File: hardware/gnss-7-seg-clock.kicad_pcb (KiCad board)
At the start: 2 copper layers, 225 x 63.5 mm, 90 parts, among them J1 USB4105-GF-A, J2 Conn_Coaxial, J3 Conn_01x03, SW1 SW_Push, SW2 SW_Push, SW3 SW_Push, SW4 SW_Push, SW5 SW_Push, U1 SA15-11GWA, U10 RP2040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

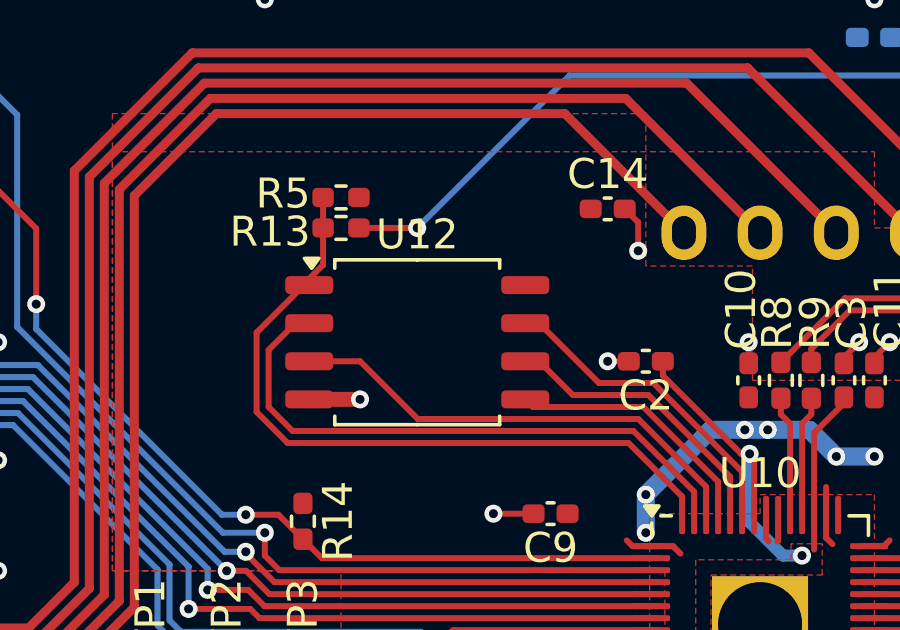
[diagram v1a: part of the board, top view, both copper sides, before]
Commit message: Update W25Q32JVSS footprint
see also: https://gitlab.com/kicad/libraries/kicad-footprint-generator/-/merge_requests/1384
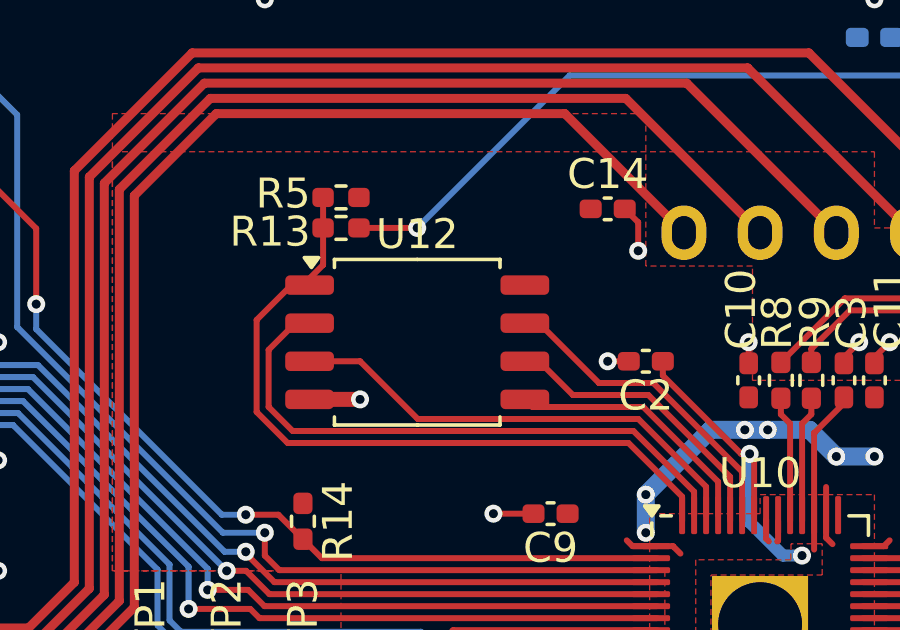
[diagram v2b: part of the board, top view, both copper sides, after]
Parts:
- U12: footprint Package_SO:SOIC-8_5.275x5.275mm_P1.27mm -> Package_SO:SOIC-8_5.3x5.3mm_P1.27mm
